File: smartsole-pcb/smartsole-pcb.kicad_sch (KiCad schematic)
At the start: 38 parts, among them U1 NINA-B306-00B, U2 BQ25185DLHR, U3 BMI270, U4 MPR121QR2

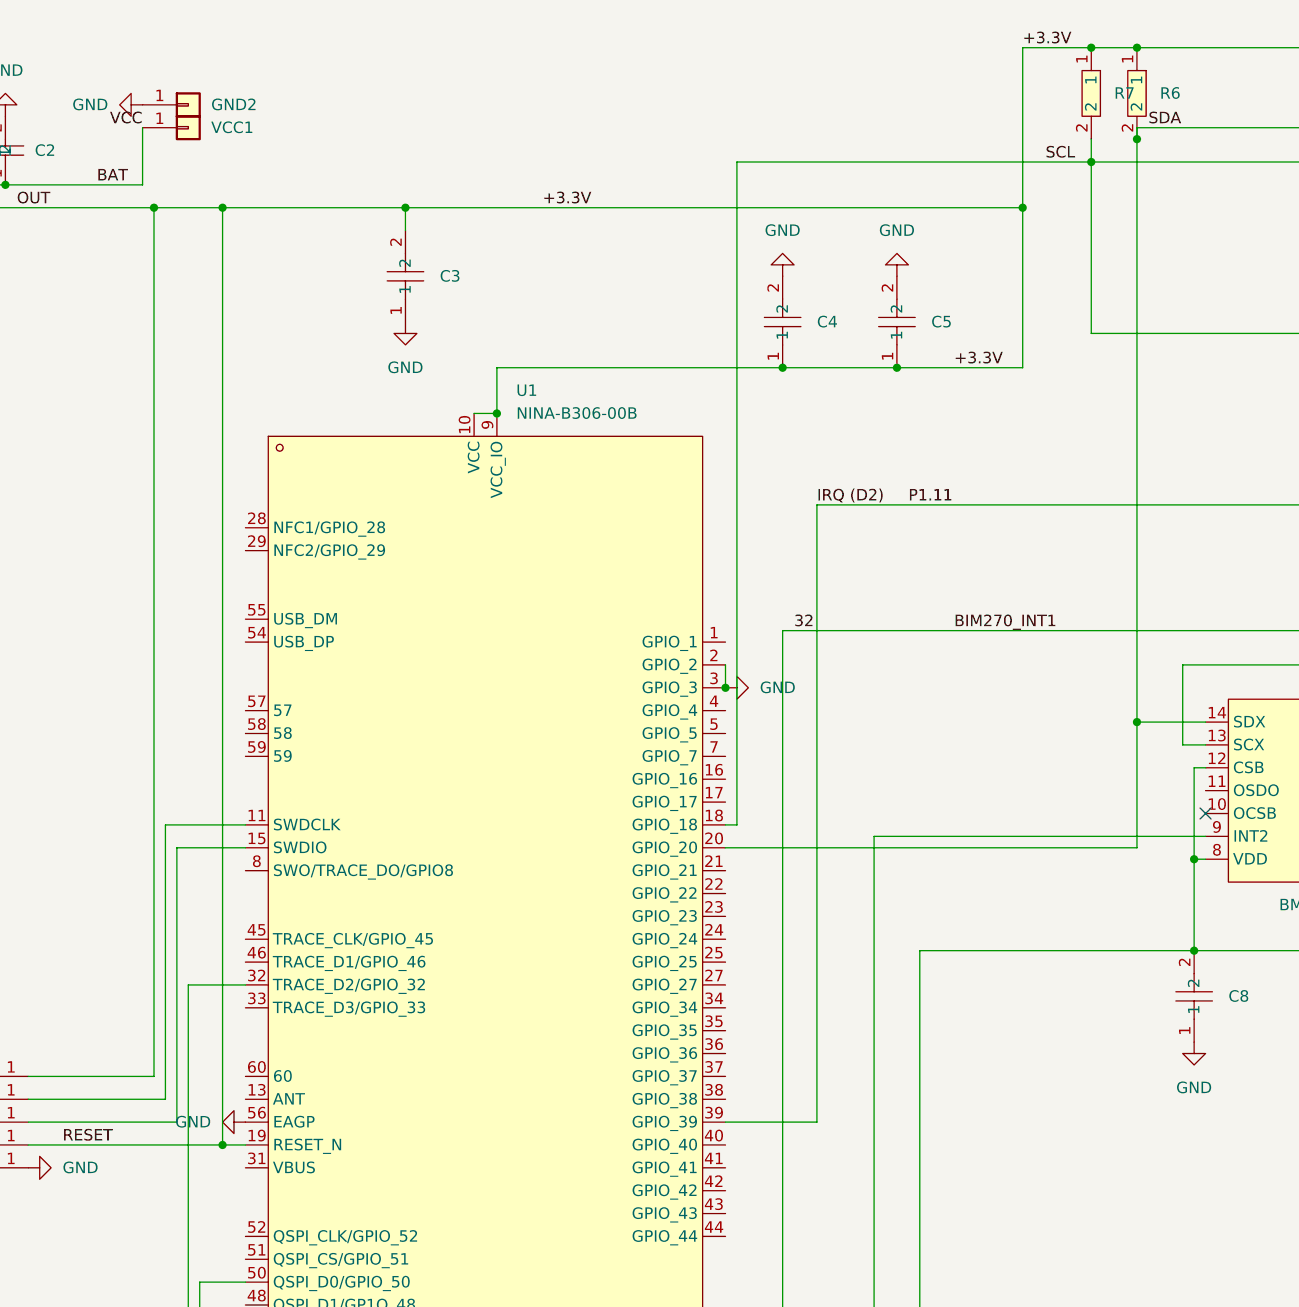
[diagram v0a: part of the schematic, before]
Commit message: began work on V1.3 - antenna moved to board edge, better GND plane, and better decoupling capacitor placement
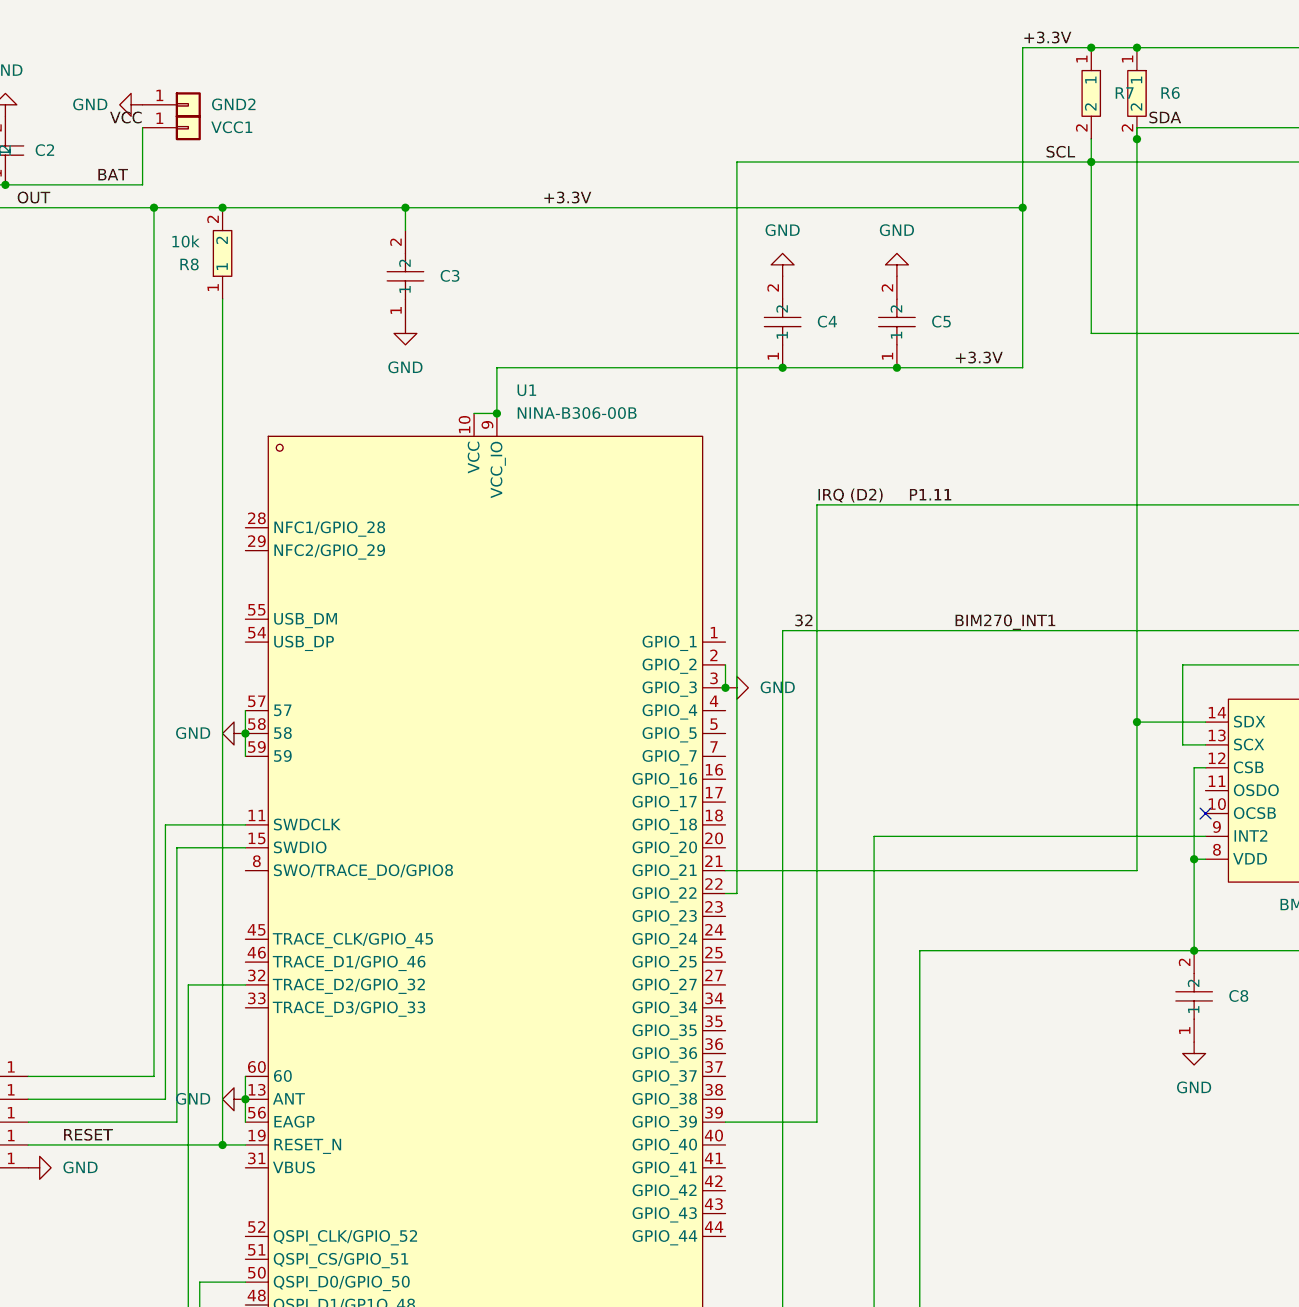
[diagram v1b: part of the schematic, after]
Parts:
- added R8: 10k, easyeda2kicad:R0805, symbol easyeda2kicad:0805W8J0103T5E
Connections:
- net +3.3V: now also R8.2; no longer RESET1.1 (Pin_1), U1.19 (RESET_N)
- net GND: now also U1.13 (ANT), U1.57, U1.58, U1.59, U1.60
- net SCL: now also U1.22 (GPIO_22); no longer U1.18 (GPIO_18)
- net SDA: now also U1.21 (GPIO_21); no longer U1.20 (GPIO_20)
- new net RESET: R8.1, RESET1.1 (Pin_1), U1.19 (RESET_N)

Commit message: V1.3 - slightly smaller
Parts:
- renumbered VCC1 to BAT_IN
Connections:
- no-connect marks 7 -> 44
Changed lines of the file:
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@@
 	)
 	(no_connect
+		(at 176.53 101.6)
+	)
+	(no_connect
+		(at 176.53 139.7)
+	)
+	(no_connect
 		(at 49.53 33.02)
 	)
 	(no_connect
+		(at 176.53 91.44)
+	)
+	(no_connect
+		(at 123.19 81.28)
+	)
+	(no_connect
+		(at 123.19 116.84)
+	)
+	(no_connect
 		(at 82.55 30.48)
 	)
 	(no_connect
+		(at 176.53 99.06)
+	)
+	(no_connect
+		(at 123.19 142.24)
+	)
+	(no_connect
+		(at 123.19 71.12)
+	)
+	(no_connect
+		(at 123.19 157.48)
+	)
+	(no_connect
 		(at 252.73 95.25)
 	)
 	(no_connect
+		(at 176.53 83.82)
+	)
+	(no_connect
+		(at 176.53 147.32)
+	)
+	(no_connect
+		(at 123.19 83.82)
+	)
+	(no_connect
+		(at 176.53 132.08)
+	)
+	(no_connect
+		(at 123.19 124.46)
+	)
+	(no_connect
+		(at 176.53 144.78)
+	)
+	(no_connect
+		(at 123.19 162.56)
+	)
+	(no_connect
+		(at 176.53 106.68)
+	)
+	(no_connect
+		(at 229.87 100.33)
+	)
+	(no_connect
 		(at 82.55 27.94)
 	)
@@
 	)
 	(no_connect
+		(at 176.53 127)
+	)
+	(no_connect
+		(at 123.19 119.38)
+	)
+	(no_connect
+		(at 123.19 109.22)
+	)
+	(no_connect
+		(at 176.53 142.24)
+	)
+	(no_connect
+		(at 176.53 116.84)
+	)
+	(no_connect
+		(at 123.19 149.86)
+	)
+	(no_connect
 		(at 252.73 97.79)
 	)
+	(no_connect
+		(at 176.53 121.92)
+	)
+	(no_connect
+		(at 176.53 134.62)
+	)
+	(no_connect
+		(at 176.53 104.14)
+	)
+	(no_connect
+		(at 176.53 124.46)
+	)
+	(no_connect
+		(at 176.53 119.38)
+	)
+	(no_connect
+		(at 176.53 129.54)
+	)
+	(no_connect
+		(at 123.19 73.66)
+	)
+	(no_connect
+		(at 176.53 114.3)
+	)
+	(no_connect
+		(at 176.53 149.86)
+	)
+	(no_connect
+		(at 176.53 93.98)
+	)
+	(no_connect
+		(at 123.19 152.4)
+	)
+	(no_connect
+		(at 238.76 121.92)
+	)
+	(no_connect
+		(at 176.53 96.52)
+	)
 	(wire
 		(pts
@@
 		(in_pos_files yes)
 		(dnp no)
-		(property "Reference" "VCC1"
+		(property "Reference" "BAT_IN"
 			(at 119.38 26.67 0)
 			(show_name no)
@@
 			(project "smartsole-pcb"
 				(path "/7ef18357-7bf1-49ca-8bce-fbd360a28ef8"
-					(reference "VCC1")
+					(reference "BAT_IN")
 					(unit 1)
 				)
